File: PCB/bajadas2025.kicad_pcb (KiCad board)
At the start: 2 copper layers, 99 x 126 mm, 10 parts, among them J2 Data/Power Connection

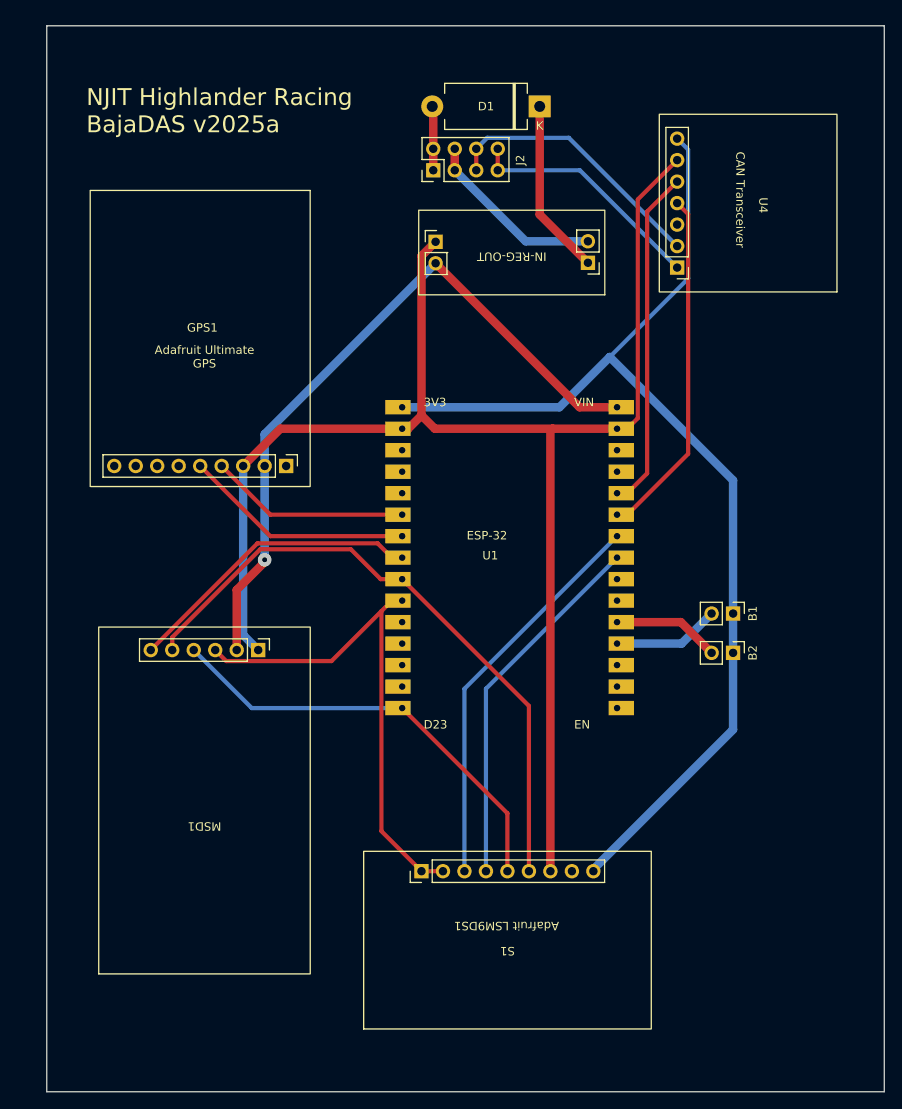
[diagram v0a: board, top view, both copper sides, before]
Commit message: Various Modifications
Update Data/Power Connection to use pads

Update spare buttons to use pads

Update spare buttons to be tied to ground (to use internal pullup)

Fix Ultimate GPS to use GPS_RX->ESP32_TX and GPS_TX-ESP32_RX

Connect GPS_FIX to an arbitrary GPIO input pin in case we want to use it in the future

Add pads for toggle switch

Add second set of pads for auxiliary aviation plug connector

Update positioning of components on PCB

Add voltage divider circuit for measuring battery voltage

Move CAN-TX and CAN-RX to standardized GPIO
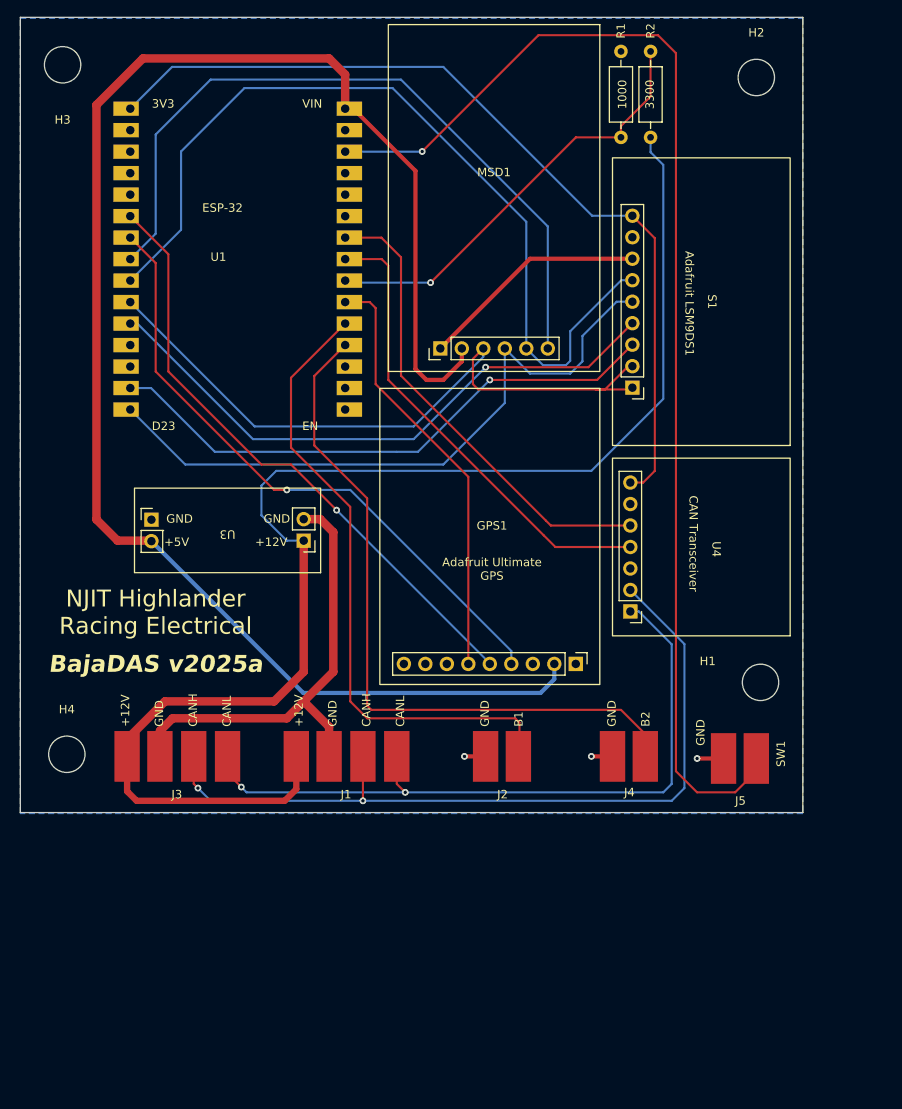
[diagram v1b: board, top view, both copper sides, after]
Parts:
- removed B1: Spare Button 1, Connector_PinHeader_2.54mm:PinHeader_1x02_P2.54mm_Vertical
- removed B2: Spare Button 2, Connector_PinHeader_2.54mm:PinHeader_1x02_P2.54mm_Vertical
- removed D1: D_Schottky, Diode_THT:D_DO-201_P12.70mm_Horizontal
- added H1: MountingHole, MountingHole:MountingHole_4.3mm_M4, F.Cu at (140.0, 103.5)
- added H2: MountingHole, MountingHole:MountingHole_4.3mm_M4, F.Cu at (139.5, 32.0)
- added H3: MountingHole, MountingHole:MountingHole_4.3mm_M4, F.Cu at (57.5, 30.5)
- added H4: MountingHole, MountingHole:MountingHole_4.3mm_M4, F.Cu at (58.0, 112.0)
- added J1: Auxiliary Data/Power Connection, BajaDAS:4pin, F.Cu at (80.0, 112.2)
- added J3: Data/Power Connection, BajaDAS:4pin, F.Cu at (60.0, 112.2)
- added J4: Spare Button 2, BajaDAS:2pin, F.Cu at (117.4, 112.2)
- added J5: Spare Toggle Switch, BajaDAS:2pin, F.Cu at (130.5, 112.5)
- added R1: 1000, Resistor_THT:R_Axial_DIN0207_L6.3mm_D2.5mm_P10.16mm_Horizontal, F.Cu at (123.5, 39.1)
- added R2: 3300, Resistor_THT:R_Axial_DIN0207_L6.3mm_D2.5mm_P10.16mm_Horizontal, F.Cu at (127.0, 39.1)
- J2: value Data/Power Connection -> Spare Button 1; footprint Connector_PinHeader_2.54mm:PinHeader_2x04_P2.54mm_Vertical -> BajaDAS:2pin
- moved MSD1 79.0 mm to (108.5, 46.2), turned to -90 degrees
- moved S1 78.9 mm to (133.0, 58.5), turned to 180 degrees
- moved J2 69.3 mm to (102.4, 112.2)
- moved U1 47.7 mm to (78.2, 35.7)
- moved U3 47.0 mm to (77.0, 85.5)
- moved GPS1 41.5 mm to (108.0, 86.2)
- moved U4 41.0 mm to (133.0, 87.5)
- renumbered IN-REG-OUT to U3
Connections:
- GPS1 pad 4: /RXD -> /TXD
- GPS1 pad 5: /TXD -> /RXD
- GPS1 pad 6: unconnected-(GPS1-FIX-Pad6) -> /GPS_FIX
- J2 pad 1: Net-(D1-A) -> GND
- J2 pad 2: Net-(D1-A) -> /B1
- U1 pad 11: unconnected-(U1-D21-Pad11) -> /CSAG
- U1 pad 14: unconnected-(U1-D22-Pad14) -> /CSM
- U1 pad 19: /B1 -> /B2
- U1 pad 20: /B2 -> /B1
- U1 pad 21: unconnected-(U1-D32-Pad21) -> /GPS_FIX
- U1 pad 22: unconnected-(U1-D33-Pad22) -> /LOW_BATT
- U1 pad 23: /CSAG -> /CTX
- U1 pad 24: /CSM -> /CRX
- U1 pad 25: /CTX -> unconnected-(U1-D27-Pad25)
- U1 pad 26: /CRX -> unconnected-(U1-D14-Pad26)
- U1 pad 28: unconnected-(U1-D13-Pad28) -> /SW1
- U1 pad 4: Net-(J1-Pin_1) -> unconnected-(U1-D2-Pad4)
- U3 pad 2: GND1 -> GND
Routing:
- net /SW1: track 0.00 -> 143.6 mm, vias 0 -> 1
- net +12V: track 20.8 -> 163.8 mm
- net +5V: track 84.4 -> 193.8 mm, vias 1 -> 0
- net GND: track 178.8 -> 89.5 mm, vias 0 -> 3
- net /B2: track 12.7 -> 83.6 mm
- net /B1: track 12.6 -> 75.3 mm
- net /CANH: track 32.1 -> 94.0 mm, vias 0 -> 2
- net /CANL: track 28.5 -> 83.5 mm, vias 0 -> 2
- net /LOW_BATT: track 0.00 -> 51.4 mm, vias 0 -> 1
- net /CS: track 35.6 -> 86.6 mm
- net /GPS_FIX: track 0.00 -> 50.5 mm
- net /RXD: track 23.7 -> 72.6 mm, vias 0 -> 1
- net /TXD: track 27.3 -> 74.3 mm, vias 0 -> 1
- net /SCK: track 75.2 -> 102.7 mm
- net /CSAG: track 43.5 -> 70.8 mm, vias 0 -> 1
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- added copper zone on B.Cu, net GND
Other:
- board size 99 x 126 mm -> 92.5 x 94 mm
- board text added: "+12V"
- board text added: "+5V"
- board text added: "1000"
- board text added: "3300"
- board text added: "B1"
- board text added: "B2"
- board text added: "BajaDAS v2025a"
- board text added: "CANH"
- board text added: "CANL"
- board text added: "GND"
- board text added: "NJIT Highlander Racing Electrical"
- board text added: "SW1"
- board text removed: "NJIT Highlander Racing BajaDAS v2025a"
